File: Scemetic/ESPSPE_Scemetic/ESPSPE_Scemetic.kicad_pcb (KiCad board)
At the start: 2 copper layers, 56 parts, among them J1 Screw_Terminal_01x02, SW1 RESET, T1 749070010, U1 DEVKIT_V1_ESP32-WROOM-32, U2 ADIN1110, Y2 CFPX-180_830105863709

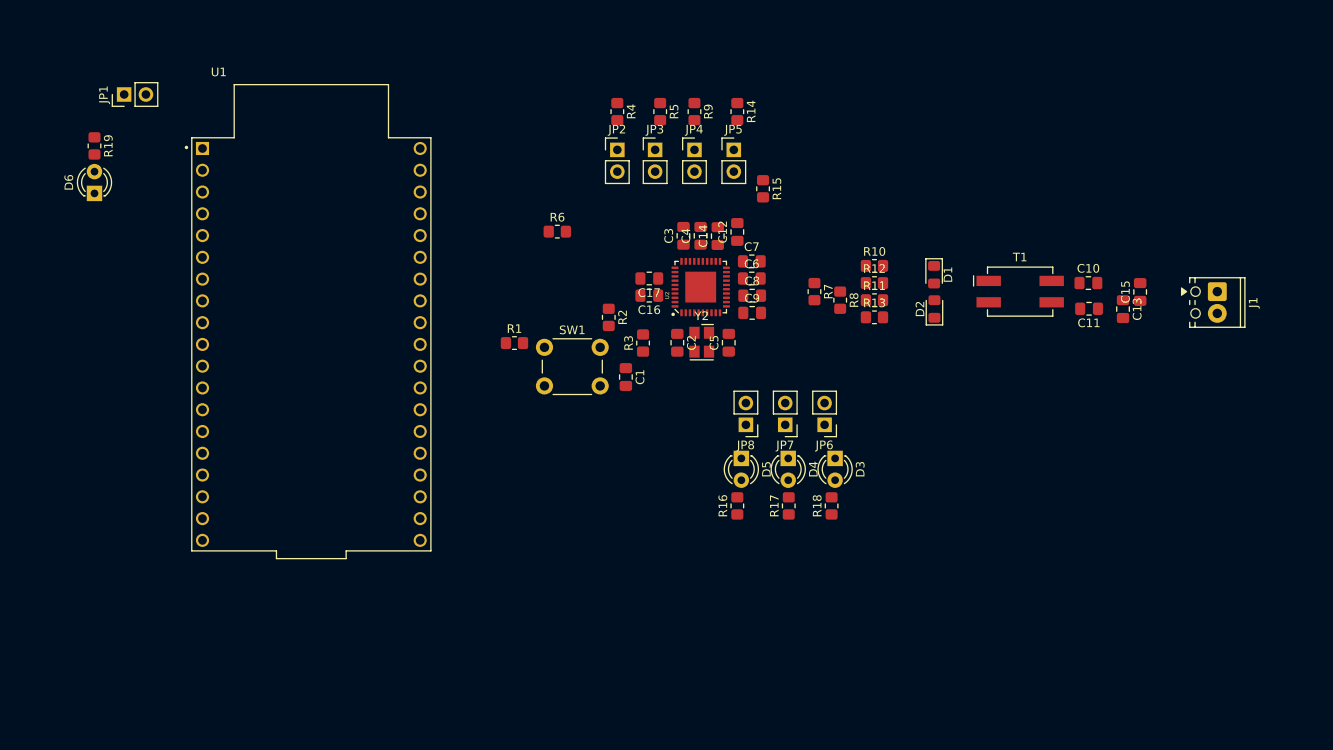
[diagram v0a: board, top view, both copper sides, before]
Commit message: Jumper der LEDs entfernt
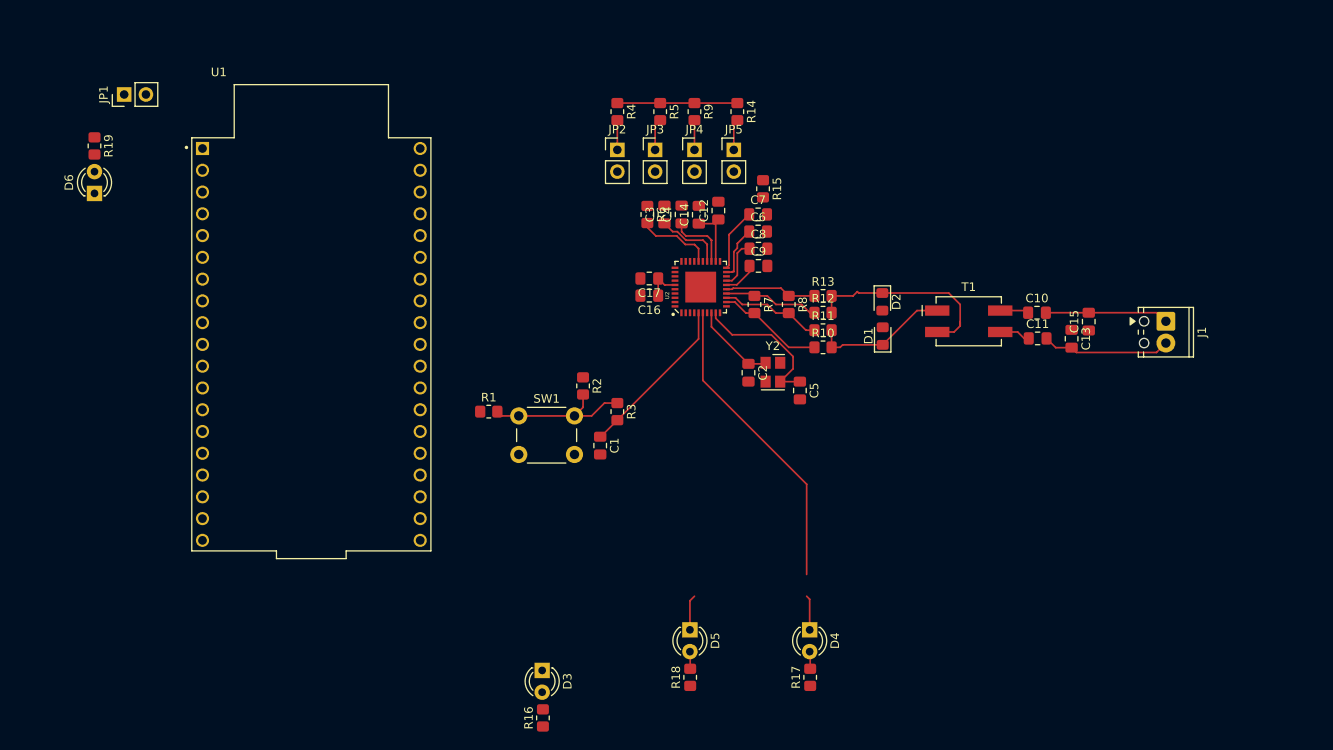
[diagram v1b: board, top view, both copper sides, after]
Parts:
- removed JP6: LED_0, Connector_PinHeader_2.54mm:PinHeader_1x02_P2.54mm_Vertical
- removed JP7: LED_1, Connector_PinHeader_2.54mm:PinHeader_1x02_P2.54mm_Vertical
- removed JP8: LINK_ST, Connector_PinHeader_2.54mm:PinHeader_1x02_P2.54mm_Vertical
- moved D3 42.2 mm to (132.2, 106.2)
- moved R16 33.6 mm to (132.3, 111.7)
- moved R18 25.9 mm to (149.5, 107.0)
- moved D5 20.9 mm to (149.5, 101.5)
- moved D4 20.2 mm to (163.4, 101.5)
- moved R17 20.2 mm to (163.5, 107.0)
- moved R10 11.2 mm to (165.0, 68.5)
- moved R6 10.7 mm to (144.5, 53.0), turned to -90 degrees
- moved C5 10.00 mm to (162.3, 73.5), turned to -90 degrees
- moved D1 9.34 mm to (172.0, 67.2), turned to 90 degrees
- moved C2 9.01 mm to (156.3, 71.5)
- moved Y2 9.01 mm to (159.2, 71.4)
- moved C1 8.54 mm to (139.0, 80.0)
- moved R1 8.54 mm to (126.0, 76.0)
- moved R2 8.54 mm to (137.0, 73.0)
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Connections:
- D3 pad 1: Net-(D3-K) -> LED_0
- D4 pad 1: Net-(D4-K) -> LED_1
- D5 pad 1: Net-(D5-K) -> LINK_ST
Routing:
- net LED_1: track 0.00 -> 39.6 mm
- net AVDD_H: track 0.00 -> 35.6 mm
- net Net-(D2-K): track 0.00 -> 23.8 mm
- net Net-(U2-~{RESET}): track 0.00 -> 19.3 mm
- net Net-(SW1-A): track 0.00 -> 17.7 mm
- net Net-(U2-XTAL_O): track 0.00 -> 17.4 mm
- net Net-(D1-K): track 0.00 -> 16.1 mm
- net Net-(U2-DLDO_1P1): track 0.00 -> 15.4 mm
- net Net-(J1-Pin_2): track 0.00 -> 15.1 mm
- net Net-(J1-Pin_1): track 0.00 -> 14.4 mm
- net Net-(U2-TXN): track 0.00 -> 12.5 mm
- net Net-(U2-RXN): track 0.00 -> 11.8 mm
- net Net-(U2-RXP): track 0.00 -> 11.2 mm
- net Net-(U2-TXP): track 0.00 -> 10.7 mm
- net Net-(U2-XTAL_I/CLK_IN): track 0.00 -> 10.1 mm
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
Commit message: Platine bis auf GND geroutet
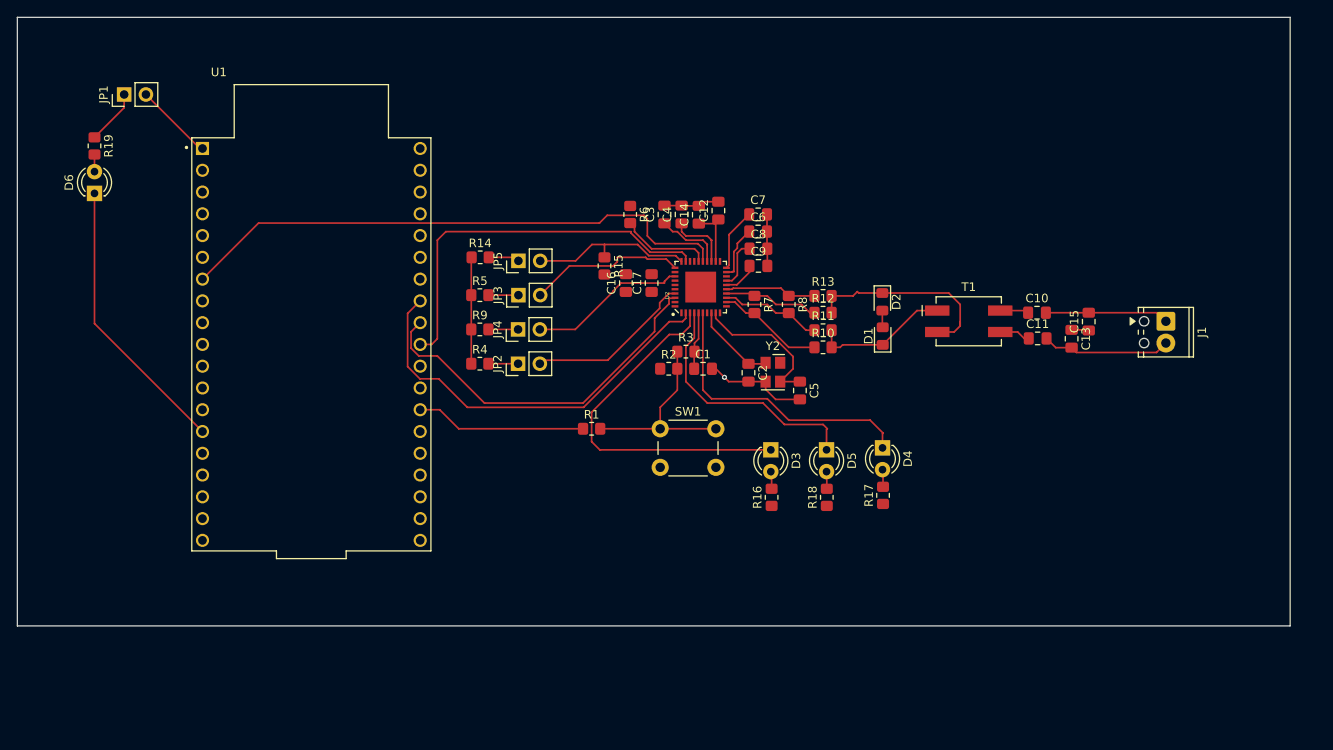
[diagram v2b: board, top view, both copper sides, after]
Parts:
- moved D3 37.1 mm to (158.9, 80.5)
- moved R16 37.1 mm to (159.0, 86.0)
- moved R9 35.7 mm to (125.0, 66.4), turned to 0 degrees
- moved R14 34.5 mm to (125.0, 58.0), turned to 0 degrees
- moved R4 33.5 mm to (125.0, 70.4), turned to 0 degrees
- moved R5 30.0 mm to (125.0, 62.4), turned to 0 degrees
- moved JP4 29.4 mm to (129.4, 66.4), turned to 90 degrees
- moved JP5 28.3 mm to (129.5, 58.4), turned to 90 degrees
- moved JP2 27.5 mm to (129.4, 70.4), turned to 90 degrees
- moved D5 26.4 mm to (165.4, 80.5)
- moved R18 26.4 mm to (165.4, 86.0)
- moved JP3 23.3 mm to (129.5, 62.4), turned to 90 degrees
- moved R17 22.9 mm to (172.0, 85.8)
- moved D4 22.9 mm to (171.9, 80.2)
- moved R15 20.6 mm to (139.5, 59.0)
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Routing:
- net INT: track 0.00 -> 65.7 mm
- net GND: track 0.00 -> 61.8 mm, vias 0 -> 1
- net MISO: track 0.00 -> 47.6 mm
- net CS: track 0.00 -> 45.1 mm
- net SCLK: track 0.00 -> 43.2 mm
- net LED_0: track 0.00 -> 42.0 mm
- net LINK_ST: track 4.14 -> 30.2 mm
- net RESET: track 0.00 -> 19.9 mm
- net MS_SEL: track 0.00 -> 19.6 mm
- net SPI_CFG1: track 0.00 -> 19.5 mm
- net SWPD_EN: track 0.00 -> 18.5 mm
- net TX2P4_EN: track 0.00 -> 18.4 mm
- net Net-(U2-~{RESET}): track 19.3 -> 6.74 mm
- net Net-(JP1-B): track 0.00 -> 9.21 mm
- net Net-(SW1-A): track 17.7 -> 24.0 mm
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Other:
- board outline added: 148.5 x 71 mm

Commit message: Z Dioden hinzugefügt
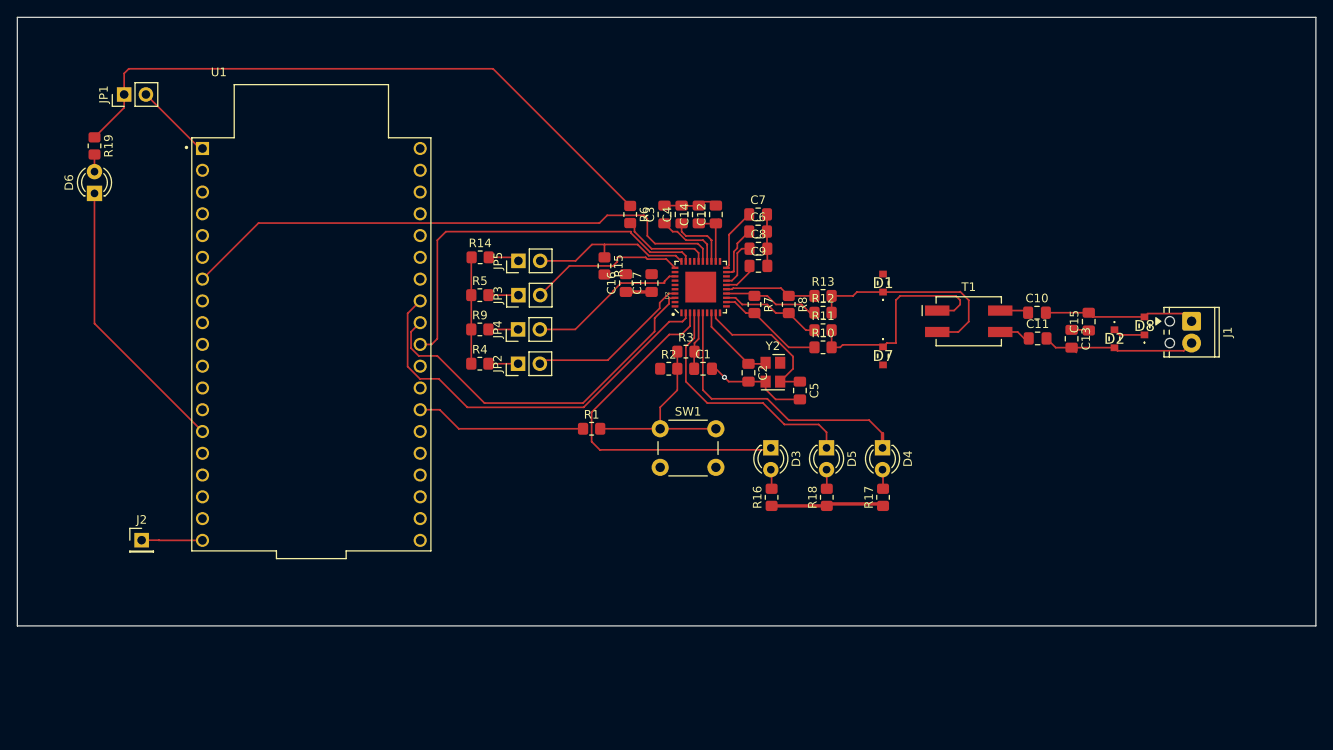
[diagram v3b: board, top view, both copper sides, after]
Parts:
- added D7: UDZUVFHTE-175.6B, KiCad_ZDiode_8pf:UDZUVFHTE1756B, F.Cu at (172.0, 69.5)
- added D8: UDZUVFHTE-175.6B, KiCad_ZDiode_8pf:UDZUVFHTE1756B, F.Cu at (202.5, 66.0)
- added J2: Conn_01x01_Pin, Connector_PinHeader_2.54mm:PinHeader_1x01_P2.54mm_Vertical, F.Cu at (85.5, 91.0)
- D1, D2: value D_Zener -> UDZUVFHTE-175.6B; footprint Diode_SMD:D_0805_2012Metric_Pad1.15x1.40mm_HandSolder -> KiCad_ZDiode_8pf:UDZUVFHTE1756B
- moved D2 27.4 mm to (199.0, 67.5), turned to 0 degrees
- moved D1 6.19 mm to (172.0, 61.0), turned to 180 degrees
- moved J1 3.00 mm to (208.0, 65.5)
- moved C12 0.54 mm to (152.5, 53.0)
- moved R17 0.23 mm to (172.0, 86.0)
- moved D3 0.23 mm to (158.9, 80.2)
- moved D5 0.23 mm to (165.4, 80.2)
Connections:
- C11 pad 2: Net-(J1-Pin_2) -> Net-(D2-A)
- C13 pad 2: Net-(J1-Pin_2) -> Net-(D2-A)
- D2 pad 2: GND -> Net-(D2-A)
- J1 pad 2: Net-(J1-Pin_2) -> Net-(D2-A)
- R10 pad 2: Net-(D1-K) -> Net-(D7-K)
- R11 pad 2: Net-(D1-K) -> Net-(D7-K)
- R12 pad 2: Net-(D2-K) -> Net-(D1-K)
- R13 pad 2: Net-(D2-K) -> Net-(D1-K)
- T1 pad 1: Net-(D1-K) -> Net-(D7-K)
- T1 pad 4: Net-(D2-K) -> Net-(D1-K)
- U1 pad 19: unconnected-(U1-EXT_5V-Pad19) -> Net-(J2-Pin_1)
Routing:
- net AVDD_H: track 36.2 -> 120.6 mm
- net Net-(D7-K): track 0.00 -> 26.1 mm
- net Net-(D2-K): track 23.8 -> 3.75 mm
- net Net-(D2-A): track 0.00 -> 18.7 mm
- net Net-(J1-Pin_2): track 15.1 -> 0.00 mm
- net Net-(D1-K): track 16.1 -> 25.3 mm
- net Net-(J2-Pin_1): track 0.00 -> 7.11 mm
- net Net-(D8-A): track 14.4 -> 17.7 mm
- net GND: track 61.8 -> 59.8 mm
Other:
- board size 148.5 x 71 mm -> 151.5 x 71 mm

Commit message: Schönifizierung des Netzwerkes; Dioden THT zu SMD gewechselt
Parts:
- D3, D4, D5, D6: footprint LED_THT:LED_D3.0mm -> LED_SMD:LED_0805_2012Metric_Pad1.15x1.40mm_HandSolder
- moved D2 1.50 mm to (199.0, 66.0)
- moved C13 1.50 mm to (194.0, 66.0)
- moved J1 1.27 mm to (208.3, 64.2)
- moved D8 1.00 mm to (202.5, 65.0)
- moved D5 0.87 mm to (165.0, 81.0)
- moved D3 0.78 mm to (159.0, 81.0)
- moved D4 0.77 mm to (172.0, 81.0)
- moved C15 0.50 mm to (196.0, 65.0)
- moved C10 0.46 mm to (190.0, 64.0)
- moved C11 0.46 mm to (190.0, 67.0)
- moved R18 0.44 mm to (165.0, 86.0)
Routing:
- net AVDD_H: track 120.6 -> 203.5 mm
- net MOSI: track 0.00 -> 67.0 mm
- net GND: track 59.8 -> 111.1 mm
- net INT: track 65.7 -> 71.2 mm
- net MISO: track 47.6 -> 50.0 mm
- net Net-(U2-DLDO_1P1): track 15.4 -> 17.6 mm
- net Net-(U2-TXP): track 10.7 -> 12.2 mm
- net LINK_ST: track 29.9 -> 28.4 mm
- net Net-(D7-K): track 26.1 -> 24.8 mm
- net Net-(U2-RXP): track 11.2 -> 12.5 mm
- net Net-(D1-K): track 25.3 -> 24.2 mm
- net Net-(D5-A): track 2.01 -> 2.97 mm
- net Net-(D4-A): track 2.02 -> 2.97 mm
- net Net-(D3-A): track 2.04 -> 2.97 mm
- net LED_0: track 42.0 -> 41.3 mm
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
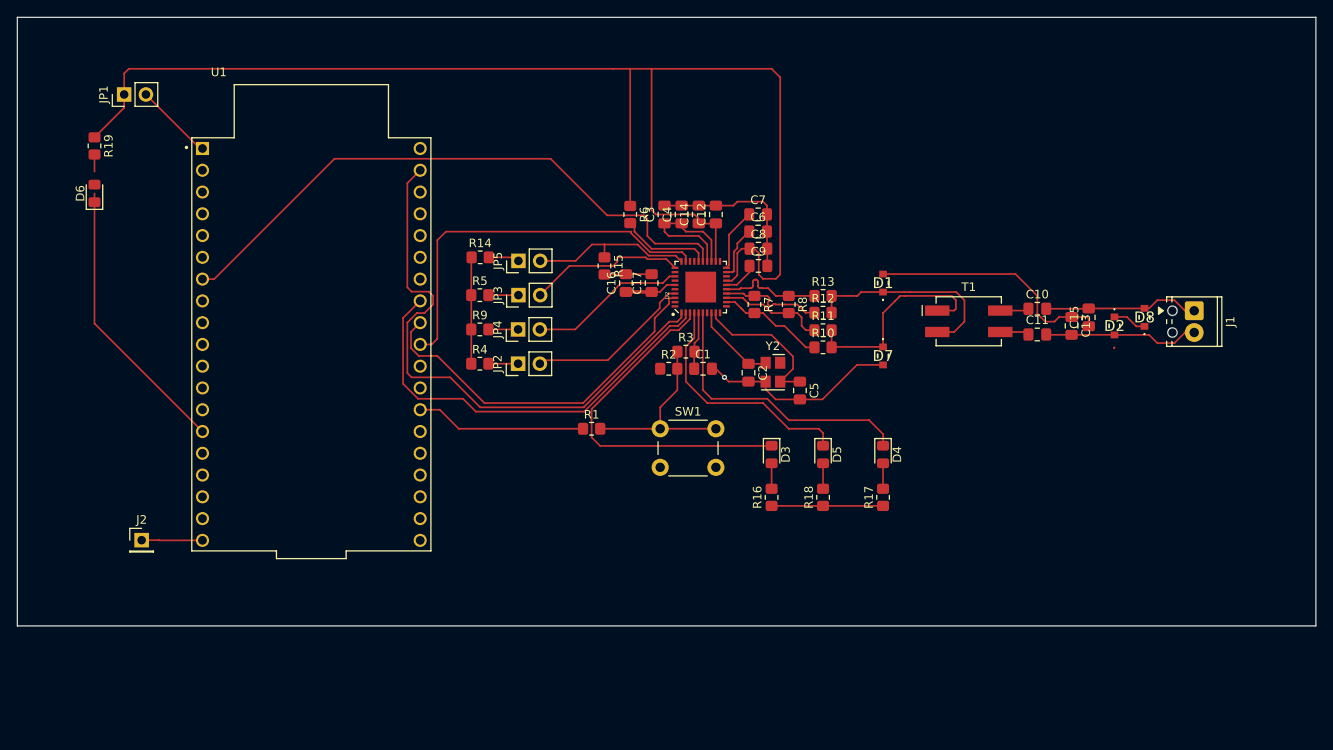
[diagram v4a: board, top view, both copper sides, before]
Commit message: Platine Bauteile kompakter angeordnet
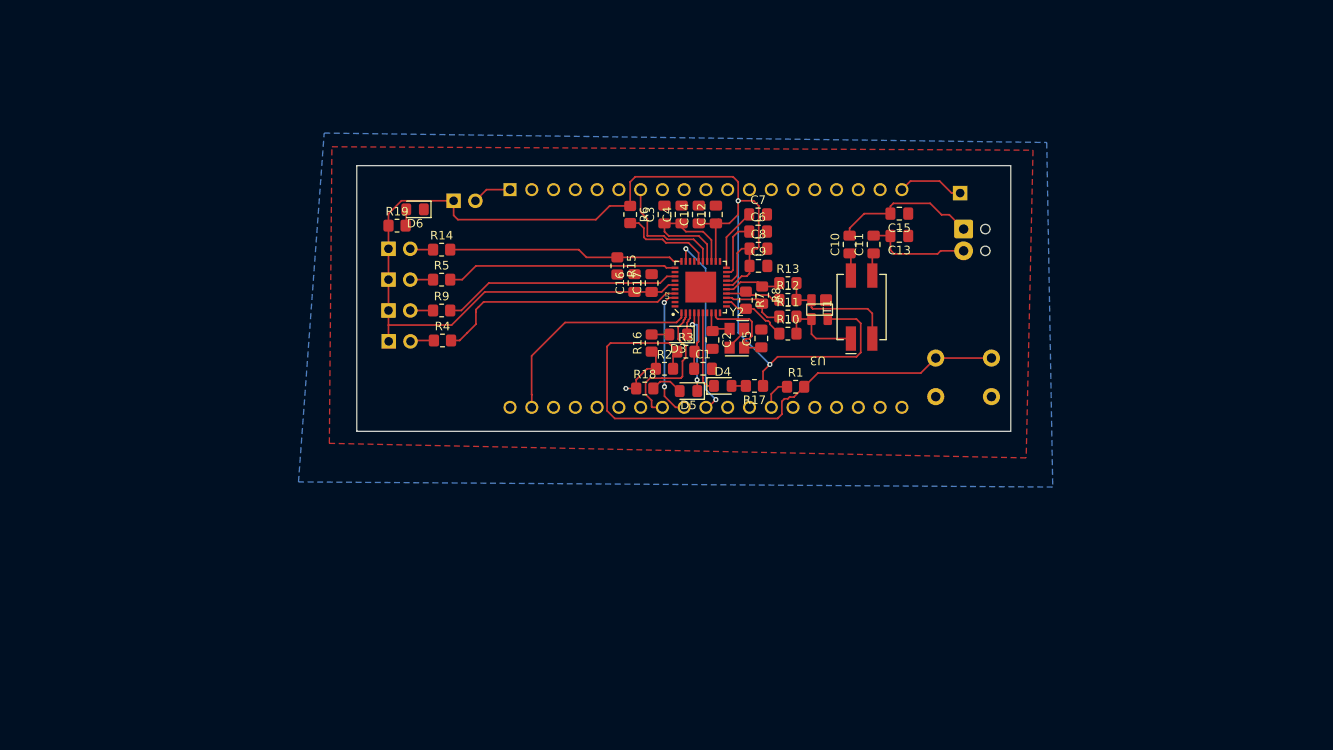
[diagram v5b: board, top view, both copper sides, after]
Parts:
- removed D1, D2, D7, D8: UDZUVFHTE-175.6B, KiCad_ZDiode_8pf:UDZUVFHTE1756B
- added U3: TVS_Diode_8240136, TVS_Diode:TVS_Diode_8240136, F.Cu at (164.6, 64.1)
- J1, J2, JP1, JP2, JP3, JP4, JP5, SW1, U1: moved to B.Cu
- moved J2 103.7 mm to (181.0, 50.5), turned to 180 degrees
- moved U1 46.3 mm to (151.3, 62.8), turned to -90 degrees
- moved JP1 40.4 mm to (121.9, 51.4), turned to -90 degrees
- moved SW1 39.5 mm to (184.7, 69.8), turned to 180 degrees
- moved D6 37.4 mm to (117.4, 52.4), turned to 180 degrees
- moved R19 36.5 mm to (115.3, 54.3), turned to 0 degrees
- moved J1 28.5 mm to (181.4, 54.7)
- moved C15 25.2 mm to (173.9, 52.9), turned to 180 degrees
- moved R18 24.4 mm to (144.2, 73.3), turned to 0 degrees
- moved R1 24.3 mm to (161.8, 73.1)
- moved C10 23.1 mm to (168.1, 56.5), turned to 90 degrees
- moved R16 22.8 mm to (145.0, 68.0)
- moved C13 22.7 mm to (173.9, 55.5), turned to 180 degrees
- moved C11 21.8 mm to (170.9, 56.5), turned to 90 degrees
- moved D4 20.3 mm to (153.3, 73.0), turned to 0 degrees
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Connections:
- JP2 pad 1: Net-(JP2-A) -> AVDD_H
- JP2 pad 2: SPI_CFG1 -> Net-(JP2-B)
- JP3 pad 1: Net-(JP3-A) -> AVDD_H
- JP3 pad 2: TX2P4_EN -> Net-(JP3-B)
- JP4 pad 1: Net-(JP4-A) -> AVDD_H
- JP4 pad 2: SWPD_EN -> Net-(JP4-B)
- JP5 pad 1: Net-(JP5-A) -> AVDD_H
- JP5 pad 2: MS_SEL -> Net-(JP5-B)
- R14 pad 1: AVDD_H -> Net-(JP5-B)
- R14 pad 2: Net-(JP5-A) -> MS_SEL
- R4 pad 1: AVDD_H -> Net-(JP2-B)
- R4 pad 2: Net-(JP2-A) -> SPI_CFG1
- R5 pad 1: AVDD_H -> Net-(JP3-B)
- R5 pad 2: Net-(JP3-A) -> TX2P4_EN
- R9 pad 1: AVDD_H -> Net-(JP4-B)
- R9 pad 2: Net-(JP4-A) -> SWPD_EN
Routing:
- net GND: track 111.1 -> 4.13 mm, vias 1 -> 0
- net INT: track 71.2 -> 14.3 mm
- net Net-(SW1-A): track 24.0 -> 67.5 mm
- net MOSI: track 67.0 -> 25.9 mm
- net LED_0: track 41.3 -> 3.03 mm
- net MISO: track 50.0 -> 17.3 mm
- net SCLK: track 43.2 -> 15.3 mm, vias 0 -> 2
- net LED_1: track 33.5 -> 9.75 mm
- net CS: track 45.1 -> 22.1 mm, vias 0 -> 2
- net AVDD_H: track 203.5 -> 182.3 mm, vias 0 -> 3
- net LINK_ST: track 28.4 -> 9.76 mm, vias 0 -> 2
- net RESET: track 19.9 -> 3.95 mm
- net Net-(U3-I/O_2): track 24.8 -> 10.4 mm
- net SPI_CFG1: track 19.5 -> 29.4 mm
- net SWPD_EN: track 18.4 -> 27.9 mm
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- added copper zone on B.Cu, net AVDD_H
- added copper zone on F.Cu, net GND
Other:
- board size 151.5 x 71 mm -> 76.3 x 31 mm
